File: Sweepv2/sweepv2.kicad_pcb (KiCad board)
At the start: 2 copper layers, 217.3 x 86.9 mm, 49 parts, among them J1 AudioJack4dpb, J2 AudioJack4dpb, SW10 SW_Push, SW11 SW_Push, SW11_r1 SW_Push, SW12 SW_Push, SW12_r1 SW_Push, SW13_r1 SW_Push, SW14 SW_Push, SW15 SW_Push, SW15_r1 SW_Push, SW16 SW_Push, SW16_r1 SW_Push, SW17 SW_Push, SW17_r1 SW_Push, SW18 SW_Push, SW18_r1 SW_Push, SW2 SW_Push, SW20 SW_Push, SW20_r1 SW_Push, SW21 SW_Push, SW21_r1 SW_Push, SW2_r1 SW_Push, SW3 SW_Push, SW3_r1 SW_Push, SW4 SW_Push, SW4_r1 SW_Push, SW5 SW_Push, SW5_r1 SW_Push, SW6 SW_Push, SW6_r1 SW_Push, SW7_r1 SW_Push, SW8 SW_Push, SW8_r1 SW_Push, SW9 SW_Push, SW9_r1 SW_Push, U1 ProMicro-kbd, U2 ProMicro-kbd

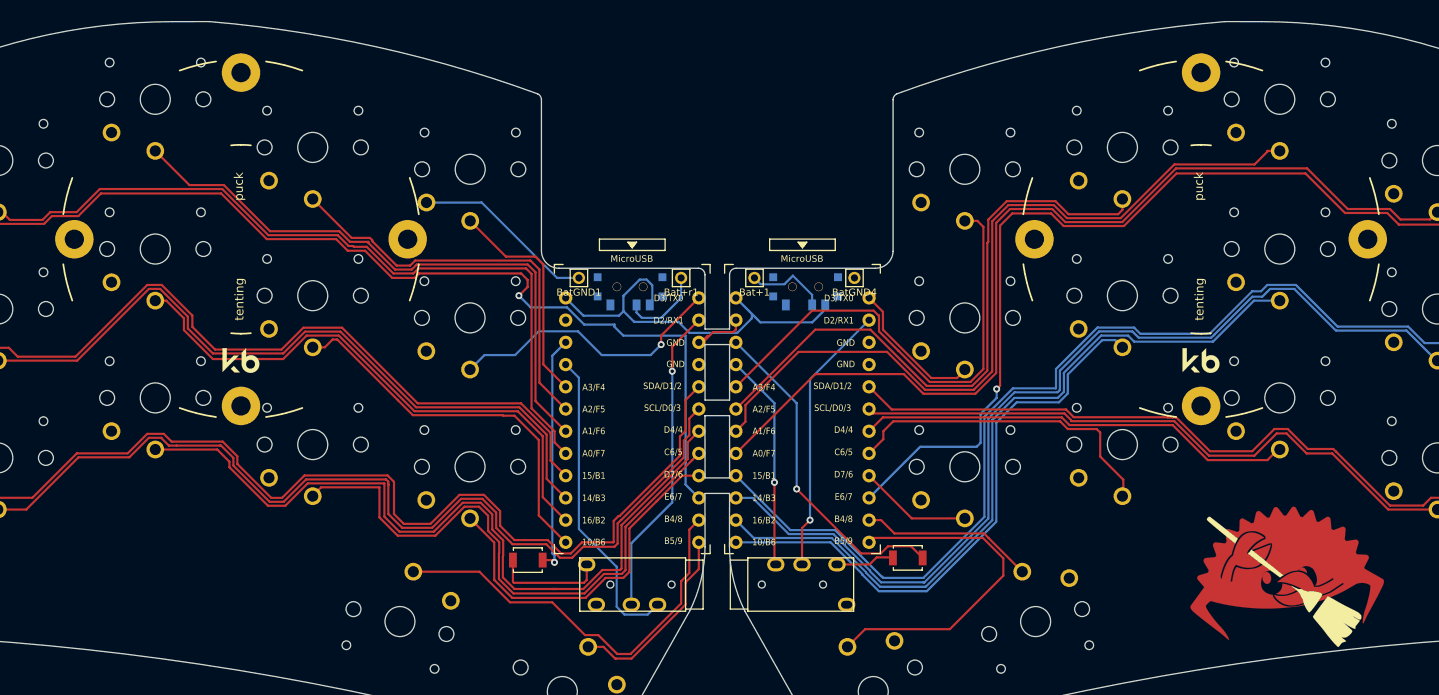
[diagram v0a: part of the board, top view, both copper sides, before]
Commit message: pcbs are flip-able for optional up-facing controllers, add top plate
allow the pcbs to be flipped so you can use a bugger battery under nice!nano (potentially) add top plate.

Untested...
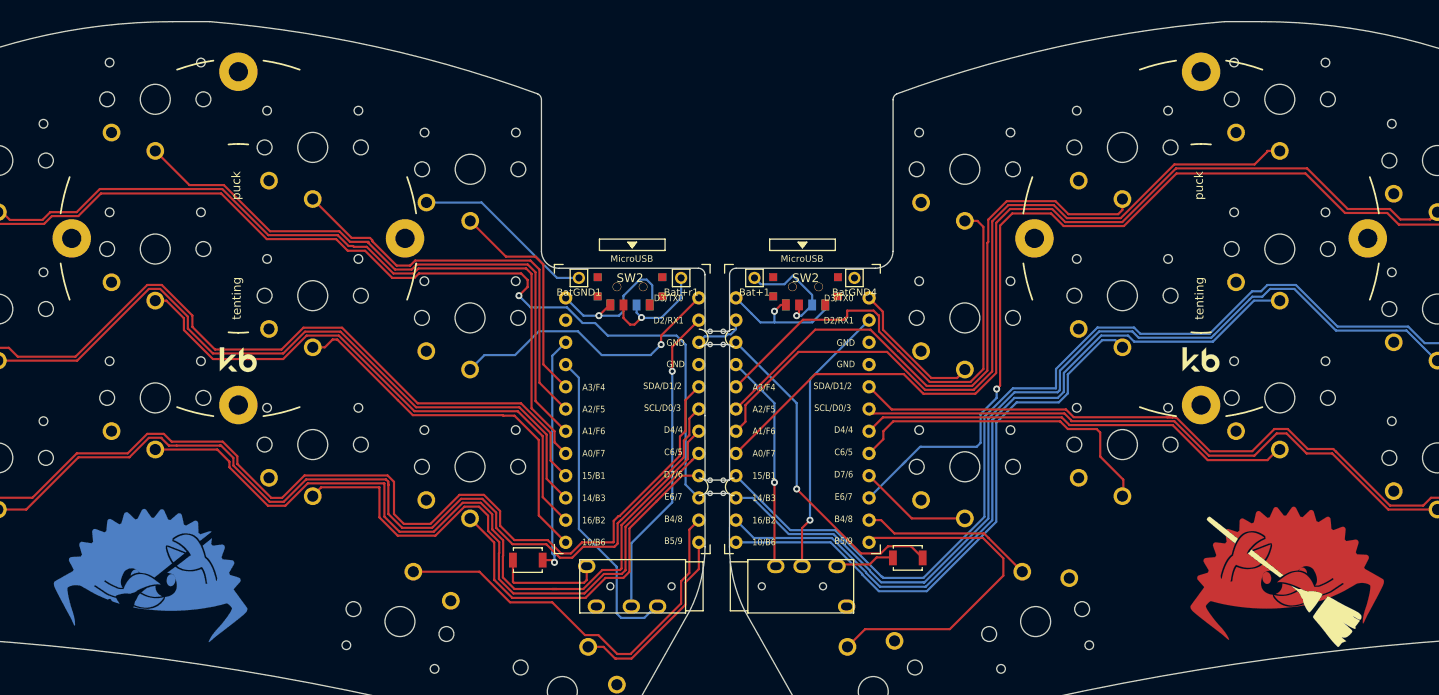
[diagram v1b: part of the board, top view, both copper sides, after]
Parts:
- added G***: LOGO, Kailh:ferris_broom, B.Cu at (58.9, 77.2)
- added SW2: SW_SPDT, Kailh:SPDT_C128955r, F.Cu at (132.3, 43.4)
- added SW2: SW_SPDT, Kailh:SPDT_C128955r, F.Cu at (112.3, 43.4)
- added mouse-bite-2mm-slot: VAL**, kbd:mouse-bite-2mm-slot-with-space-for-track, F.Cu at (122.2, 49.3)
- added mouse-bite-2mm-slot: VAL**, kbd:mouse-bite-2mm-slot-with-space-for-track, F.Cu at (122.2, 66.3)
- U1, U2: footprint kbd:ProMicro_v3 -> kbd:ProMicro_v3_flip
- moved REF** 0.32 mm to (67.5, 37.9)
- moved J1 0.20 mm to (125.7, 77.7)
- moved J2 0.20 mm to (118.6, 77.7)
- moved REF** 0.10 mm to (177.5, 37.9)
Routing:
- net raw: track 45.5 -> 33.3 mm, vias 0 -> 2
- net BT+_r: track 9.45 -> 13.7 mm, vias 0 -> 1
- net BT+: track 9.35 -> 13.0 mm, vias 0 -> 1
- net gnd: track 48.4 -> 47.0 mm
- net vcc: track 60.6 -> 61.4 mm
- net Switch1: track 131.8 -> 131.1 mm
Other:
- outline, holes or cut-outs redrawn

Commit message: resets and trrs
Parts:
- added RSW1: SW_Push, kbd:SW_SPST_B3U-1000P, B.Cu at (100.6, 74.7)
- added RSW2: SW_Push, kbd:SW_SPST_B3U-1000P, B.Cu at (144.0, 74.4)
- J1, J2: footprint Kailh:TRRS-PJ-320A -> Kailh:TRRS-PJ-DPB2
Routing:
- net gnd: track 47.0 -> 68.2 mm, vias 0 -> 1
- net vcc: track 61.4 -> 70.6 mm
- net Switch18: track 35.7 -> 40.4 mm
- net Switch18_r: track 31.1 -> 35.7 mm
- net reset_r: track 38.0 -> 40.7 mm, vias 1 -> 2
- net Switch14: track 67.5 -> 69.6 mm
- net Switch9_r: track 66.7 -> 68.5 mm
- net Switch8_r: track 87.6 -> 89.3 mm
- net reset: track 27.3 -> 28.8 mm
- net Switch6_r: track 135.2 -> 136.2 mm
- net Switch7_r: track 110.3 -> 111.3 mm
- net Switch13: track 92.1 -> 91.2 mm
- net Switch15: track 41.3 -> 41.8 mm
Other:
- board text added: "Face down"

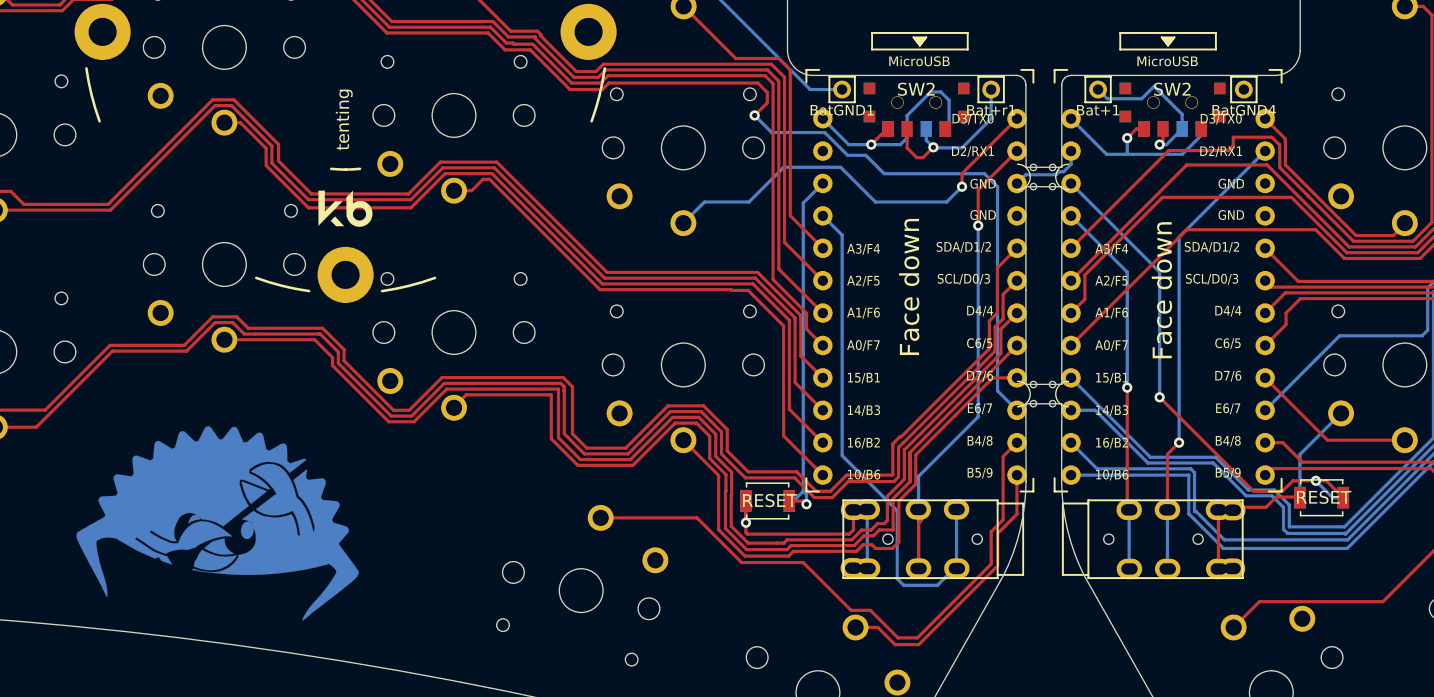
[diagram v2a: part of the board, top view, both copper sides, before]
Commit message: remove all the reversible bits
back to one sided.
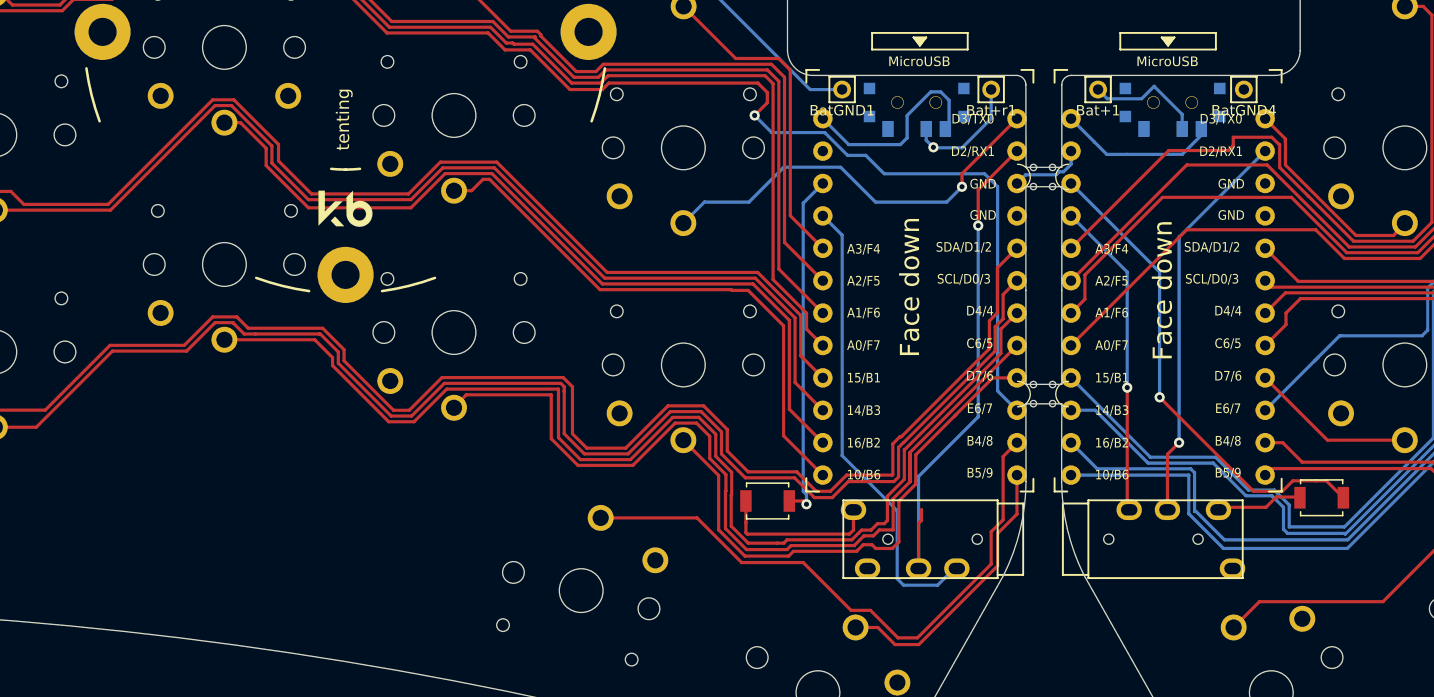
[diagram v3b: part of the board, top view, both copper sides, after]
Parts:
- removed the G*** at (58.9, 77.2)
- removed the RSW1 at (100.6, 74.7)
- removed the RSW2 at (144.0, 74.4)
- removed the SW2 at (132.3, 43.4)
- removed the SW2 at (112.3, 43.4)
- J1, J2: footprint Kailh:TRRS-PJ-DPB2 -> Kailh:TRRS-PJ-320A
- SW10: footprint Kailh:SW_PG1350_nonrev_DPB -> Kailh:SW_PG1350_rev_DPB
- U1, U2: footprint kbd:ProMicro_v3_flip -> kbd:ProMicro_v3
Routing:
- net gnd: track 68.2 -> 47.1 mm, vias 1 -> 0
- net vcc: track 70.6 -> 61.4 mm
- net raw: track 33.3 -> 28.6 mm, vias 2 -> 0
- net Switch18_r: track 35.7 -> 31.1 mm
- net BT+_r: track 13.7 -> 9.45 mm
- net BT+: track 13.0 -> 9.35 mm, vias 1 -> 0
- net reset_r: track 40.7 -> 38.0 mm, vias 2 -> 1
- net reset: track 28.8 -> 27.3 mm

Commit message: Refactor repository and fix breakaway tabs
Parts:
- added ?: , , F.Cu at (86.7, 24.0)
- added ?: , , B.Cu at (35.9, 45.3)
- mouse-bite-2mm-slot (x2): footprint kbd:mouse-bite-2mm-slot-with-space-for-track -> Duckyb-Parts:mouse-bite-5mm-slot-with-space-for-track
- moved mouse-bite-2mm-slot 22.7 mm to (127.5, 71.4)
- moved mouse-bite-2mm-slot 13.2 mm to (127.5, 54.2)
- moved BatGND4 7.46 mm to (143.4, 47.5)
- moved REF** 7.46 mm to (183.0, 43.0)
- moved RSW2 7.46 mm to (149.5, 79.5)
- moved SW12_r1 7.46 mm to (156.0, 52.1)
- moved SW17_r1 7.46 mm to (156.0, 69.1)
- moved SW6_r1 7.46 mm to (156.0, 35.1)
- moved U2 7.46 mm to (137.4, 64.3)
- moved Bat+1 7.46 mm to (132.0, 47.5)
- moved J1 7.46 mm to (131.2, 82.8)
- moved SW18_r1 7.46 mm to (210.0, 68.1)
- moved SW8_r1 7.46 mm to (210.0, 51.1)
- moved SW_POWER1 7.46 mm to (137.8, 48.5)
- moved SW11_r1 7.46 mm to (174.0, 49.5)
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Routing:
- net gnd: track 47.1 -> 41.2 mm
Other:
- board size 217.3 x 86.9 mm -> 217.1 x 86.9 mm

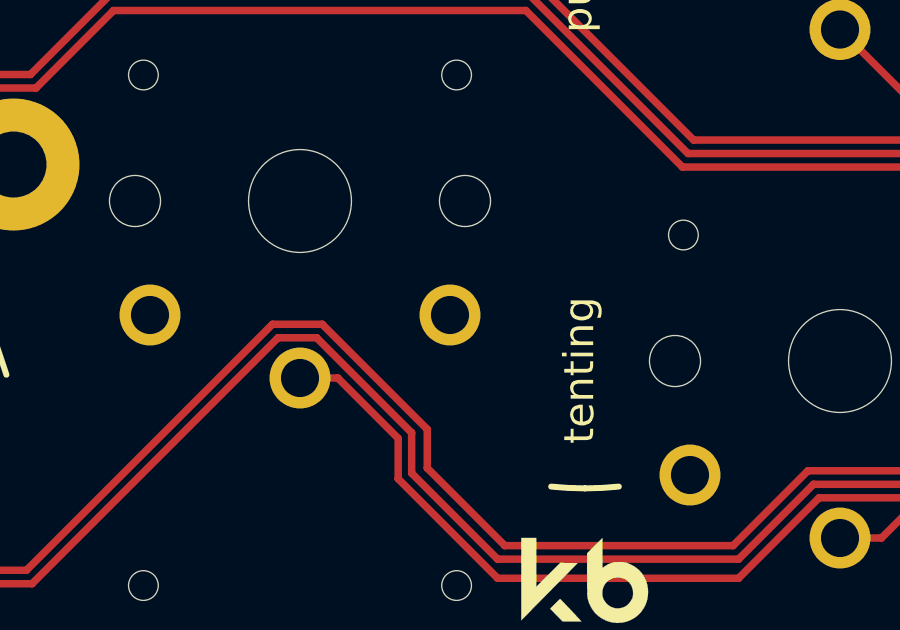
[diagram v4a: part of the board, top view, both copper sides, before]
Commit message: replace reversible switch footprint
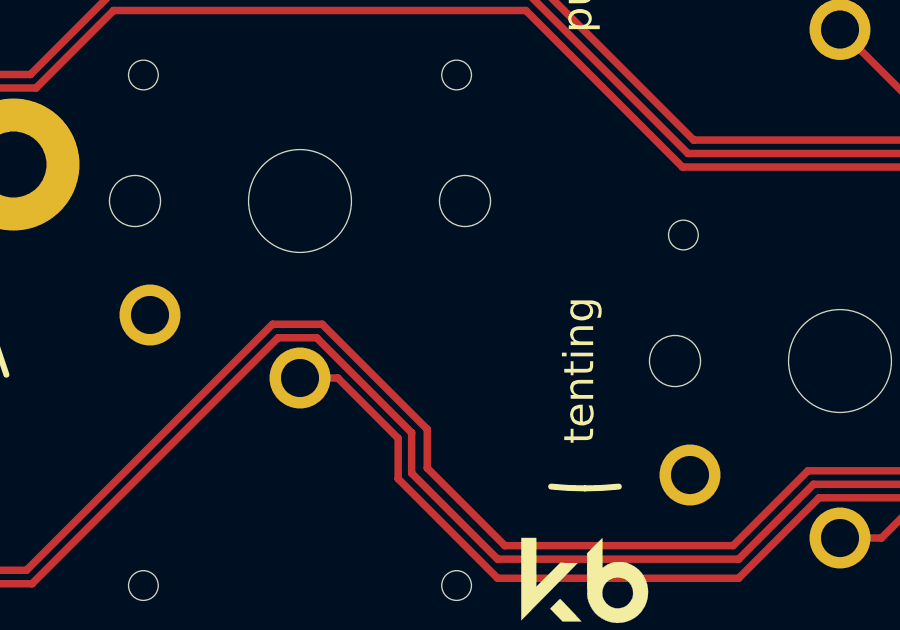
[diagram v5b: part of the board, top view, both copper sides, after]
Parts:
- SW10: footprint Kailh:SW_PG1350_rev_DPB -> Kailh:SW_PG1350_nonrev_DPB
